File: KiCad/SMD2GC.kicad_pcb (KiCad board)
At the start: 2 copper layers, 35.3 x 31.2 mm, 3 parts, among them J1 Conn_01x06, J2 DE9_Plug

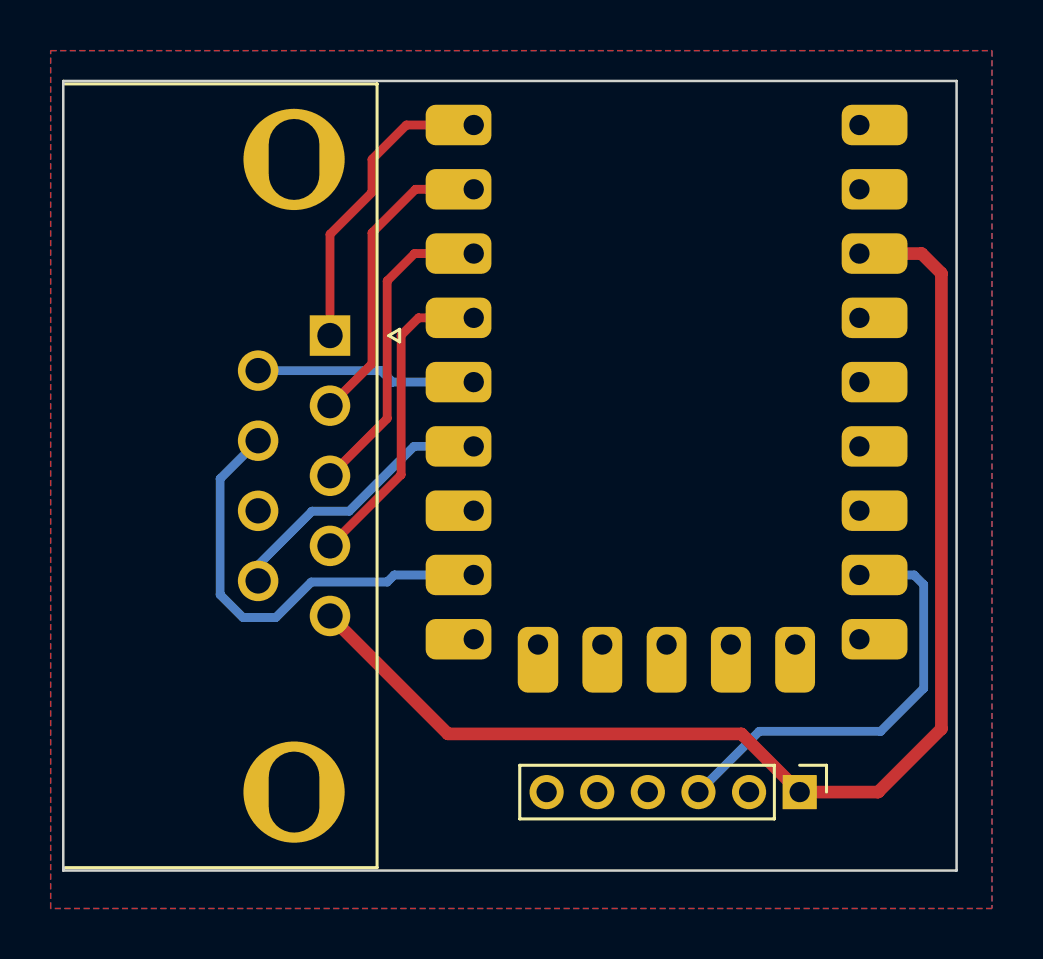
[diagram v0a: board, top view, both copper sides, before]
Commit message: Update schematic for USB VBUS +5V power from GameCube rumble power.
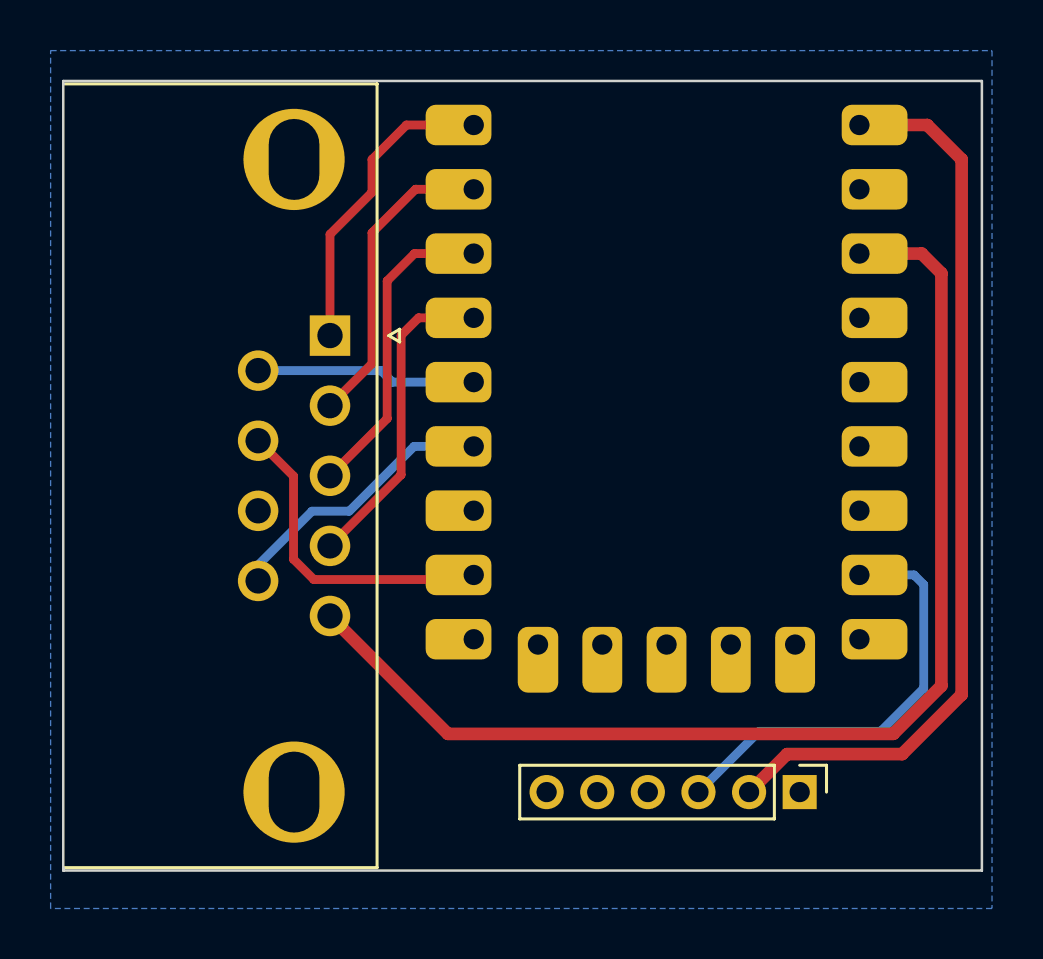
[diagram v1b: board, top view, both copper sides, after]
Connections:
- J1 pad 1: /3V3 -> unconnected-(J1-Pin_1-Pad1)
- J1 pad 4: /GND -> unconnected-(J1-Pin_4-Pad4)
- J1 pad 5: /GND -> unconnected-(J1-Pin_5-Pad5)
- J1 pad 6: /N/C -> /GND
- RZ1 pad 32: unconnected-(RZ1-5V-Pad32) -> /5V
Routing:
- net /5V: track 0.00 -> 35.7 mm
- net /SMD_SELECT: track 17.8 -> 12.8 mm
- net /3V3: track 49.6 -> 46.7 mm
- removed copper zone on F.Cu, net /GND
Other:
- board size 35.3 x 31.2 mm -> 36.3 x 31.2 mm
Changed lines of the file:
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@@
 	(net 3 "/3V3")
 	(net 4 "/5V")
-	(net 5 "/N{slash}C")
+	(net 5 "unconnected-(J1-Pin_5-Pad5)")
 	(net 6 "/SMD_D1")
 	(net 7 "/SMD_D4")
@@
 	(net 18 "unconnected-(RZ1-GP6-Pad6)")
 	(net 19 "unconnected-(RZ1-GP26-Pad26)")
-	(net 20 "unconnected-(RZ1-5V-Pad32)")
+	(net 20 "unconnected-(J1-Pin_4-Pad4)")
 	(net 21 "unconnected-(RZ1-GP9-Pad9)")
 	(net 22 "unconnected-(RZ1-GP8-Pad8)")
@@
 	(net 24 "unconnected-(RZ1-GP27-Pad27)")
 	(net 25 "unconnected-(RZ1-GP12-Pad12)")
+	(net 26 "unconnected-(J1-Pin_1-Pad1)")
 	(footprint "Connector_Dsub:DSUB-9_Male_Horizontal_P2.77x2.84mm_EdgePinOffset7.70mm_Housed_MountingHolesOffset9.12mm"
 		(layer "F.Cu")
@@
 			(layers "*.Cu" "*.Mask")
 			(remove_unused_layers no)
-			(net 3 "/3V3")
+			(net 26 "unconnected-(J1-Pin_1-Pad1)")
 			(pinfunction "Pin_1")
-			(pintype "passive")
+			(pintype "passive+no_connect")
 		)
 		(pad "2" thru_hole oval
@@
 			(net 4 "/5V")
 			(pinfunction "Pin_2")
-			(pintype "passive+no_connect")
+			(pintype "passive")
 		)
 		(pad "3" thru_hole oval
@@
 			(layers "*.Cu" "*.Mask")
 			(remove_unused_layers no)
-			(net 2 "/GND")
+			(net 20 "unconnected-(J1-Pin_4-Pad4)")
 			(pinfunction "Pin_4")
-			(pintype "passive")
+			(pintype "passive+no_connect")
 		)
 		(pad "5" thru_hole oval
@@
 			(layers "*.Cu" "*.Mask")
 			(remove_unused_layers no)
-			(net 2 "/GND")
+			(net 5 "unconnected-(J1-Pin_5-Pad5)")
 			(pinfunction "Pin_5")
-			(pintype "passive")
+			(pintype "passive+no_connect")
 		)
 		(pad "6" thru_hole oval
@@
 			(layers "*.Cu" "*.Mask")
 			(remove_unused_layers no)
-			(net 5 "/N{slash}C")
+			(net 2 "/GND")
 			(pinfunction "Pin_6")
-			(pintype "passive+no_connect")
+			(pintype "passive")
 		)
 		(model "${KICAD8_3DMODEL_DIR}/Connector_PinHeader_2.00mm.3dshapes/PinHeader_1x06_P2.00mm_Vertical.wrl"
@@
 			(remove_unused_layers no)
 			(roundrect_rratio 0.25)
-			(net 20 "unconnected-(RZ1-5V-Pad32)")
+			(net 4 "/5V")
 			(pinfunction "5V")
-			(pintype "power_in+no_connect")
+			(pintype "power_in")
 		)
 	)
 	(gr_rect
 		(start 53.2 78.9)
-		(end 88.5 110.1)
+		(end 89.5 110.1)
 		(stroke
 			(width 0.1)
@@
 	)
 	(segment
-		(start 82.3 107)
-		(end 80 104.7)
-		(width 0.5)
-		(layer "F.Cu")
-		(net 3)
-	)
-	(segment
-		(start 68.4 104.7)
-		(end 63.740331 100.040331)
-		(width 0.5)
-		(layer "F.Cu")
-		(net 3)
-	)
-	(segment
-		(start 85.4 107)
-		(end 87.9 104.5)
-		(width 0.5)
-		(layer "F.Cu")
-		(net 3)
-	)
-	(segment
-		(start 87.9 104.5)
+		(start 87.9 102.8)
 		(end 87.9 86.5)
 		(width 0.5)
@@
 	)
 	(segment
-		(start 80 104.7)
-		(end 68.4 104.7)
-		(width 0.5)
-		(layer "F.Cu")
-		(net 3)
-	)
-	(segment
-		(start 82.3 107)
-		(end 85.4 107)
+		(start 68.4 104.7)
+		(end 86 104.7)
 		(width 0.5)
 		(layer "F.Cu")
@@
 	)
 	(segment
+		(start 86 104.7)
+		(end 87.9 102.8)
+		(width 0.5)
+		(layer "F.Cu")
+		(net 3)
+	)
+	(segment
+		(start 63.740331 100.040331)
+		(end 68.4 104.7)
+		(width 0.5)
+		(layer "F.Cu")
+		(net 3)
+	)
+	(segment
 		(start 87.9 86.5)
 		(end 87.12 85.72)
@@
 	)
 	(segment
+		(start 87.34 80.64)
+		(end 84.66 80.64)
+		(width 0.5)
+		(layer "F.Cu")
+		(net 4)
+	)
+	(segment
+		(start 88.7 82)
+		(end 87.34 80.64)
+		(width 0.5)
+		(layer "F.Cu")
+		(net 4)
+	)
+	(segment
+		(start 80.3 107)
+		(end 81.8 105.5)
+		(width 0.5)
+		(layer "F.Cu")
+		(net 4)
+	)
+	(segment
+		(start 81.8 105.5)
+		(end 86.35 105.5)
+		(width 0.5)
+		(layer "F.Cu")
+		(net 4)
+	)
+	(segment
+		(start 88.7 103.15)
+		(end 88.7 82)
+		(width 0.5)
+		(layer "F.Cu")
+		(net 4)
+	)
+	(segment
+		(start 86.35 105.5)
+		(end 88.7 103.15)
+		(width 0.5)
+		(layer "F.Cu")
+		(net 4)
+	)
+	(segment
 		(start 65.4 84.9)
 		(end 67.12 83.18)
@@
 	)
 	(segment
-		(start 60.3 100.1)
-		(end 61.6 100.1)
-		(width 0.35)
-		(layer "B.Cu")
+		(start 69.24 98.6)
+		(end 69.42 98.42)
+		(width 0.35)
+		(layer "F.Cu")
 		(net 12)
 	)
 	(segment
+		(start 62.3 97.8)
+		(end 63.1 98.6)
+		(width 0.35)
+		(layer "F.Cu")
+		(net 12)
+	)
+	(segment
+		(start 63.1 98.6)
+		(end 69.24 98.6)
+		(width 0.35)
+		(layer "F.Cu")
+		(net 12)
+	)
+	(segment
+		(start 62.3 94.515)
+		(end 62.3 97.8)
+		(width 0.35)
+		(layer "F.Cu")
+		(net 12)
+	)
+	(segment
 		(start 60.900331 93.115331)
-		(end 59.4 94.615662)
-		(width 0.35)
-		(layer "B.Cu")
-		(net 12)
-	)
-	(segment
-		(start 59.4 94.615662)
-		(end 59.4 99.2)
-		(width 0.35)
-		(layer "B.Cu")
-		(net 12)
-	)
-	(segment
-		(start 66.28 98.42)
-		(end 69.42 98.42)
-		(width 0.35)
-		(layer "B.Cu")
-		(net 12)
-	)
-	(segment
-		(start 66 98.7)
-		(end 66.28 98.42)
-		(width 0.35)
-		(layer "B.Cu")
-		(net 12)
-	)
-	(segment
-		(start 61.6 100.1)
-		(end 63 98.7)
-		(width 0.35)
-		(layer "B.Cu")
-		(net 12)
-	)
-	(segment
-		(start 63 98.7)
-		(end 66 98.7)
-		(width 0.35)
-		(layer "B.Cu")
-		(net 12)
-	)
-	(segment
-		(start 59.4 99.2)
-		(end 60.3 100.1)
-		(width 0.35)
-		(layer "B.Cu")
+		(end 62.3 94.515)
+		(width 0.35)
+		(layer "F.Cu")
 		(net 12)
 	)
@@
 		(net 2)
 		(net_name "/GND")
-		(layers "F&B.Cu")
+		(layer "B.Cu")
 		(hatch edge 0.5)
 		(connect_pads
